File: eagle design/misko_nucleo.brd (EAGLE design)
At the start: 115 x 115 mm, 135 parts, among them CN1 LiPo Battery, IC1 MC1525TT, IC10 LTC4425, IC101 ADXL345, IC102 74HCT1G32GW, IC11 SP3012-04UTG, IC2 ORG1510-MK4, IC3 TPS63031, IC4 FT230XS, IC5 RN4678_BT_MODULE, IC6 FM25W256-SOIC, IC7 MICROSD_SPI_MODE, IC8 DS1394U-33+, IC9 MAX6818, Q1 ABM3B-8MHZ-10-1-U-T, Q2 BSS84, Q3 LFXTAL016178R, SW1 MICROJOYSTICK, SW2 PB6156RSL, SW3 PB6156RSL, U1 SN74LVC1G3157DBVR - BT switch, U2 ATMEGA1281-16AU, U3 TPS3808G33DBVT, U4 TMP36GRTZ, U5 MCP73871-2AAI/ML, U6 SN74LVC1G3157DBVR - GPS switch, X1 FH12-30S-0.5SH

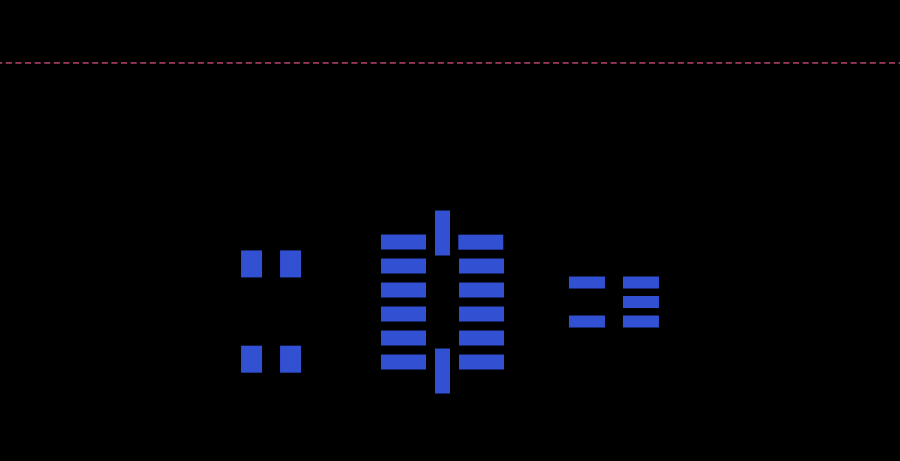
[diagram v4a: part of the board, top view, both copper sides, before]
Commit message: in main.c & sch/brd: - ditched dedicated SPI CS pullup resistors and switched to stm32 built-in pullups
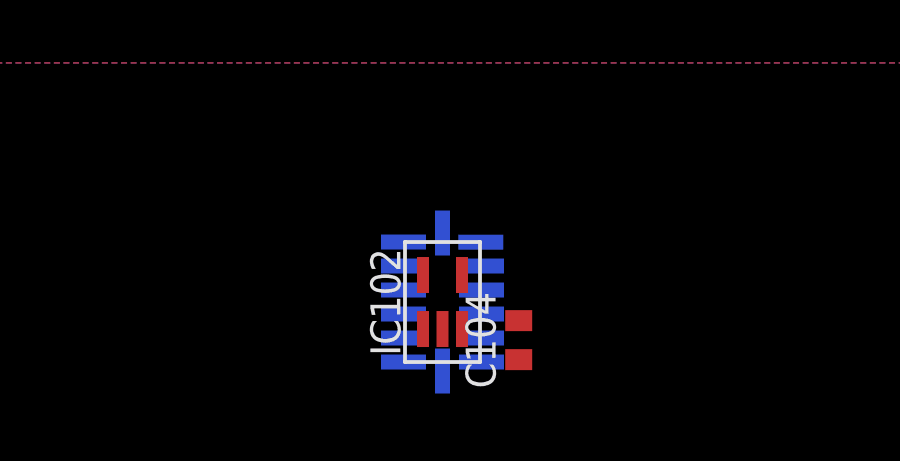
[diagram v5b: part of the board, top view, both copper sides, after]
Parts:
- removed R101: 10k, rcl:R0402
- moved C104 8.28 mm to (17.1, -15.2), flipped to the top, turned to 90 degrees
- moved IC102 5.71 mm to (14.6, -14.0), flipped to the top, turned to 0 degrees
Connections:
- net 3V3: no longer R101.2
- net ADXL345_CS: no longer R101.1
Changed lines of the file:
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@@
 <grid distance="25" unitdist="mil" unit="mm" style="lines" multiple="1" display="yes" altdistance="0.005" altunitdist="mm" altunit="mm"/>
 <layers>
-<layer number="1" name="Top" color="4" fill="1" visible="no" active="yes"/>
+<layer number="1" name="Top" color="4" fill="1" visible="yes" active="yes"/>
 <layer number="2" name="Route2" color="1" fill="3" visible="no" active="no"/>
 <layer number="3" name="Route3" color="4" fill="3" visible="no" active="no"/>
@@
 <layer number="19" name="Unrouted" color="6" fill="1" visible="yes" active="yes"/>
 <layer number="20" name="Dimension" color="14" fill="1" visible="yes" active="yes"/>
-<layer number="21" name="tPlace" color="7" fill="1" visible="no" active="yes"/>
+<layer number="21" name="tPlace" color="7" fill="1" visible="yes" active="yes"/>
 <layer number="22" name="bPlace" color="7" fill="1" visible="yes" active="yes"/>
-<layer number="23" name="tOrigins" color="15" fill="1" visible="no" active="yes"/>
+<layer number="23" name="tOrigins" color="15" fill="1" visible="yes" active="yes"/>
 <layer number="24" name="bOrigins" color="15" fill="1" visible="yes" active="yes"/>
 <layer number="25" name="tNames" color="7" fill="1" visible="no" active="yes"/>
-<layer number="26" name="bNames" color="7" fill="1" visible="yes" active="yes"/>
+<layer number="26" name="bNames" color="7" fill="1" visible="no" active="yes"/>
 <layer number="27" name="tValues" color="7" fill="1" visible="no" active="yes"/>
 <layer number="28" name="bValues" color="7" fill="1" visible="no" active="yes"/>
 <layer number="29" name="tStop" color="7" fill="3" visible="no" active="yes"/>
-<layer number="30" name="bStop" color="7" fill="6" visible="yes" active="yes"/>
+<layer number="30" name="bStop" color="7" fill="6" visible="no" active="yes"/>
 <layer number="31" name="tCream" color="7" fill="4" visible="no" active="yes"/>
 <layer number="32" name="bCream" color="7" fill="5" visible="no" active="yes"/>
@@
 <layer number="37" name="tTest" color="7" fill="1" visible="no" active="yes"/>
 <layer number="38" name="bTest" color="7" fill="1" visible="no" active="yes"/>
-<layer number="39" name="tKeepout" color="4" fill="11" visible="no" active="yes"/>
+<layer number="39" name="tKeepout" color="4" fill="11" visible="yes" active="yes"/>
 <layer number="40" name="bKeepout" color="1" fill="11" visible="yes" active="yes"/>
-<layer number="41" name="tRestrict" color="4" fill="10" visible="no" active="yes"/>
+<layer number="41" name="tRestrict" color="4" fill="10" visible="yes" active="yes"/>
 <layer number="42" name="bRestrict" color="1" fill="10" visible="yes" active="yes"/>
 <layer number="43" name="vRestrict" color="2" fill="10" visible="yes" active="yes"/>
@@
 <layer number="49" name="Reference" color="7" fill="1" visible="no" active="yes"/>
 <layer number="50" name="dxf" color="7" fill="1" visible="no" active="no"/>
-<layer number="51" name="tDocu" color="7" fill="1" visible="no" active="yes"/>
+<layer number="51" name="tDocu" color="7" fill="1" visible="yes" active="yes"/>
 <layer number="52" name="bDocu" color="7" fill="1" visible="yes" active="yes"/>
 <layer number="53" name="tGND_GNDA" color="7" fill="9" visible="no" active="no"/>
@@
 <attribute name="VALUE" x="0" y="0" size="1.27" layer="27" align="top-left"/>
 </element>
-<element name="C104" library="rcl" package="C0402" value="0.1u / 16V" x="8.89" y="-15.875" smashed="yes" rot="MR0">
-<attribute name="NAME" x="8.89" y="-14.605" size="1" layer="26" rot="MR0" align="center"/>
-<attribute name="VALUE" x="10.16" y="-18.415" size="1.27" layer="28" rot="MR0"/>
+<element name="C104" library="rcl" package="C0402" value="0.1u / 16V" x="17.145" y="-15.24" smashed="yes" rot="R90">
+<attribute name="NAME" x="15.875" y="-15.24" size="1" layer="25" rot="R90" align="center"/>
+<attribute name="VALUE" x="19.685" y="-16.51" size="1.27" layer="27" rot="R90"/>
 </element>
 <element name="IC101" library="ADXL345 Accelerometer" package="LGA14" value="ADXL345" x="14.605" y="-13.97" smashed="yes" rot="MR0">
@@
 <attribute name="VALUE" x="14.605" y="-17.72" size="1" layer="28" rot="MR0" align="center"/>
 </element>
-<element name="IC102" library="74HCT1G32GW - OR Gate" package="SOT353/5" value="74HCT1G32GW" x="20.32" y="-13.97" smashed="yes" rot="MR270">
-<attribute name="NAME" x="20.32" y="-12.065" size="1" layer="26" font="vector" rot="MR0" align="center"/>
-<attribute name="VALUE" x="20.32" y="-15.97" size="1" layer="28" font="vector" rot="MR0" align="center"/>
-</element>
-<element name="R101" library="rcl" package="R0402" value="10k" x="8.89" y="-12.7" smashed="yes" rot="MR0">
-<attribute name="NAME" x="8.89" y="-11.43" size="1" layer="26" rot="MR0" align="center"/>
-<attribute name="VALUE" x="9.525" y="-15.24" size="1.27" layer="28" rot="MR0"/>
+<element name="IC102" library="74HCT1G32GW - OR Gate" package="SOT353/5" value="74HCT1G32GW" x="14.605" y="-13.97" smashed="yes">
+<attribute name="NAME" x="12.7" y="-13.97" size="1" layer="25" font="vector" rot="R90" align="center"/>
+<attribute name="VALUE" x="16.605" y="-13.97" size="1" layer="27" font="vector" rot="R90" align="center"/>
 </element>
 </elements>
@@
 <contactref element="C104" pad="2"/>
 <contactref element="IC102" pad="GND"/>
-<wire x1="15.905" y1="-15.17" x2="8.24" y2="-15.875" width="0" layer="19" extent="16-16"/>
-<wire x1="15.905" y1="-14.37" x2="15.905" y2="-15.17" width="0" layer="19" extent="16-16"/>
+<wire x1="15.905" y1="-14.37" x2="17.145" y2="-14.59" width="0" layer="19" extent="16-16"/>
+<wire x1="15.905" y1="-15.17" x2="15.905" y2="-14.37" width="0" layer="19" extent="16-16"/>
+<wire x1="15.255" y1="-14.87" x2="15.905" y2="-15.17" width="0" layer="19" extent="1-16"/>
 <wire x1="15.905" y1="-12.77" x2="15.905" y2="-14.37" width="0" layer="19" extent="16-16"/>
-<wire x1="21.22" y1="-14.62" x2="15.905" y2="-14.37" width="0" layer="19" extent="16-16"/>
 <wire x1="5.79" y1="25.36" x2="15.905" y2="-12.77" width="0" layer="19" extent="16-16"/>
 <wire x1="90.25" y1="18" x2="66.75" y2="12.66" width="0" layer="19" extent="1-1"/>
@@
 <contactref element="IC101" pad="VCC"/>
 <contactref element="IC102" pad="VCC"/>
-<contactref element="R101" pad="2"/>
 <wire x1="15.881" y1="-11.975" x2="11.43" y2="33.02" width="0" layer="19" extent="1-16"/>
-<wire x1="19.42" y1="-13.32" x2="15.881" y2="-11.975" width="0" layer="19" extent="16-16"/>
-<wire x1="15.905" y1="-15.97" x2="15.881" y2="-11.975" width="0" layer="19" extent="16-16"/>
-<wire x1="9.54" y1="-15.875" x2="15.905" y2="-15.97" width="0" layer="19" extent="16-16"/>
-<wire x1="8.24" y1="-12.7" x2="9.54" y2="-15.875" width="0" layer="19" extent="16-16"/>
+<wire x1="13.955" y1="-13.07" x2="15.881" y2="-11.975" width="0" layer="19" extent="1-16"/>
+<wire x1="15.905" y1="-15.97" x2="13.955" y2="-13.07" width="0" layer="19" extent="1-16"/>
+<wire x1="17.145" y1="-15.89" x2="15.905" y2="-15.97" width="0" layer="19" extent="16-16"/>
 </signal>
 <signal name="NRST" class="2">
@@
 <contactref element="IC101" pad="!CS!"/>
 <contactref element="IC102" pad="A"/>
-<contactref element="R101" pad="1"/>
-<wire x1="21.22" y1="-13.97" x2="56.515" y2="33.02" width="0" layer="19" extent="1-16"/>
-<wire x1="14.605" y1="-16.27" x2="21.22" y2="-13.97" width="0" layer="19" extent="16-16"/>
-<wire x1="9.54" y1="-12.7" x2="14.605" y2="-16.27" width="0" layer="19" extent="16-16"/>
+<wire x1="14.605" y1="-14.87" x2="56.515" y2="33.02" width="0" layer="19" extent="1-1"/>
+<wire x1="14.605" y1="-16.27" x2="14.605" y2="-14.87" width="0" layer="19" extent="1-16"/>
 </signal>
 <signal name="GPS_WKUP" class="2">
@@
 <wire x1="56.555" y1="15.2" x2="56.515" y2="15.24" width="0.25" layer="1"/>
 <contactref element="IC102" pad="B"/>
-<wire x1="21.22" y1="-13.32" x2="56.515" y2="15.24" width="0" layer="19" extent="1-16"/>
+<wire x1="13.955" y1="-14.87" x2="56.515" y2="15.24" width="0" layer="19" extent="1-1"/>
 </signal>
 <signal name="PB6" class="2">
@@
 <contactref element="IC101" pad="SDA"/>
 <contactref element="IC102" pad="Y"/>
-<wire x1="13.305" y1="-11.97" x2="19.42" y2="-14.62" width="0" layer="19" extent="16-16"/>
+<wire x1="15.255" y1="-13.07" x2="13.305" y2="-11.97" width="0" layer="19" extent="1-16"/>
 </signal>
 <signal name="ADXL345:ADXL345_INT2">

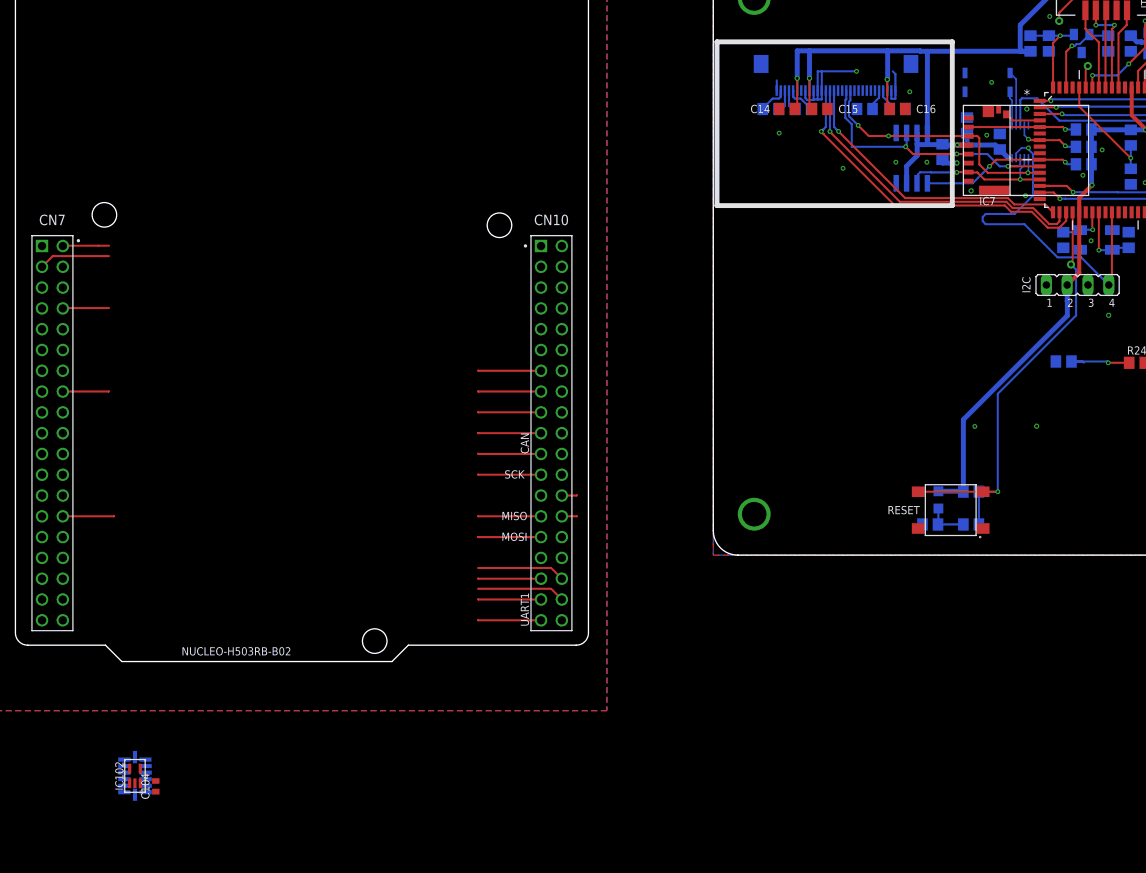
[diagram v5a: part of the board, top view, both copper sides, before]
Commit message: in brd & sch: - added FeRAM module
- created and tested fm25w256 driver
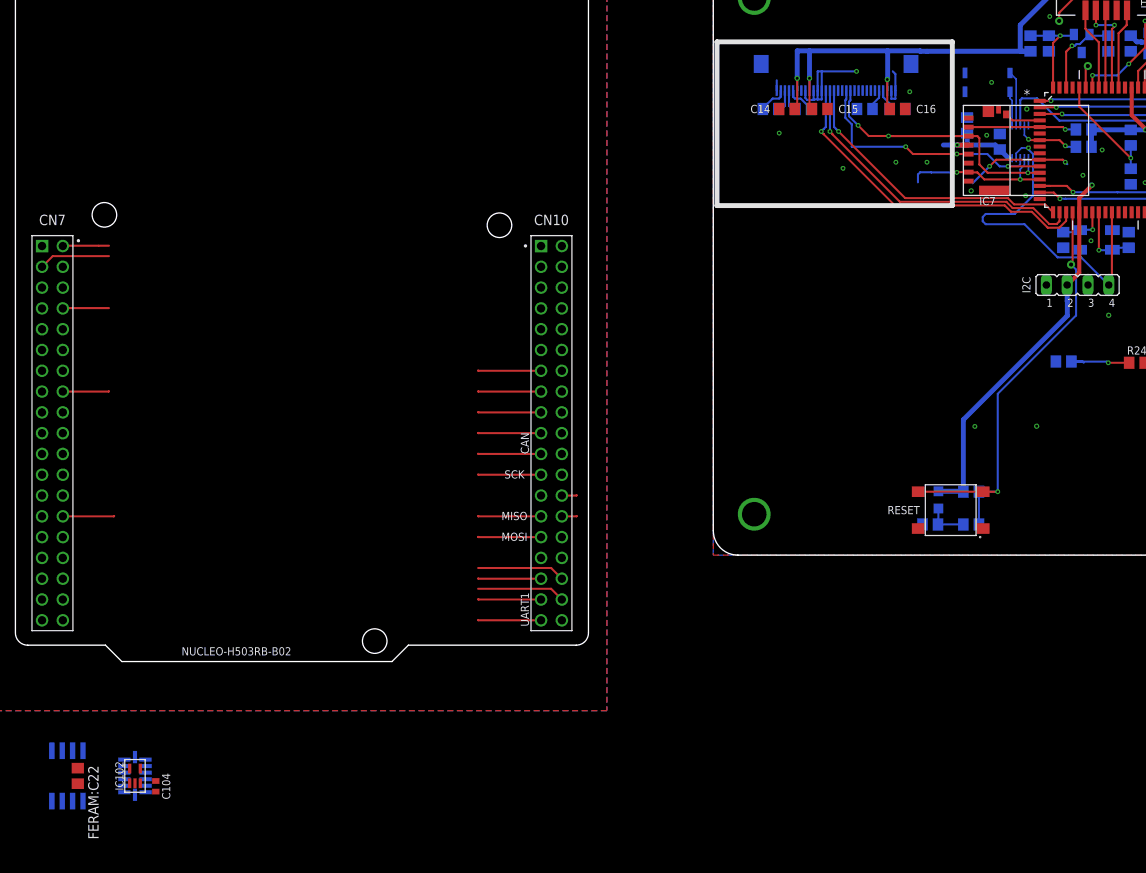
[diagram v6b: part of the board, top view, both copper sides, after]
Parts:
- removed C22: 0.1µF, rcl:C0805
- removed IC6: FM25W256-SOIC, FM25W256 FERAM:SOIC08
- removed R18: 10k, rcl:R0805
- added FERAM:C22: 0.1u / 16V, rcl:C0805
- added FERAM:IC1: FM25W256, FM25W256 FERAM:SOIC08
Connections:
- removed net SPI_FRAM_CS: BRD1.CN10_13
- new net SPI1_FRAM_CS: BRD1.CN10_13, FERAM:IC1.!CS!
- net 3V3: now also FERAM:C22.1, FERAM:IC1.!HOLD!, FERAM:IC1.!WP!, FERAM:IC1.VCC
- net GND: now also FERAM:C22.2, FERAM:IC1.GND; no longer C22.2, IC6.GND
- net SPI1_MISO: now also FERAM:IC1.SO
- net SPI1_MOSI: now also FERAM:IC1.SI
- net SPI1_SCK: now also FERAM:IC1.SCK
- net SPI_MISO_PIN: no longer IC6.SO
- net SPI_MOSI_PIN: no longer IC6.SI
- net SPI_SCK_PIN: no longer IC6.SCK
- net SPI_SS_FRAM_PIN: no longer IC6.!CS!, R18.1
- net VCC: no longer C22.1, IC6.!HOLD!, IC6.!WP!, IC6.VCC, R18.2
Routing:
- net VCC: track 448.3 -> 422.3 mm
- net SPI_FRAM_CS: track 7.71 -> 0.00 mm
- net SPI1_FRAM_CS: track 0.00 -> 7.71 mm
- net SPI_SS_FRAM_PIN: track 19.7 -> 13.0 mm
- net GND: track 49.4 -> 47.2 mm, vias 44 -> 43
- net SPI_SCK_PIN: track 36.9 -> 35.3 mm
- net SPI_MOSI_PIN: track 34.3 -> 33.7 mm

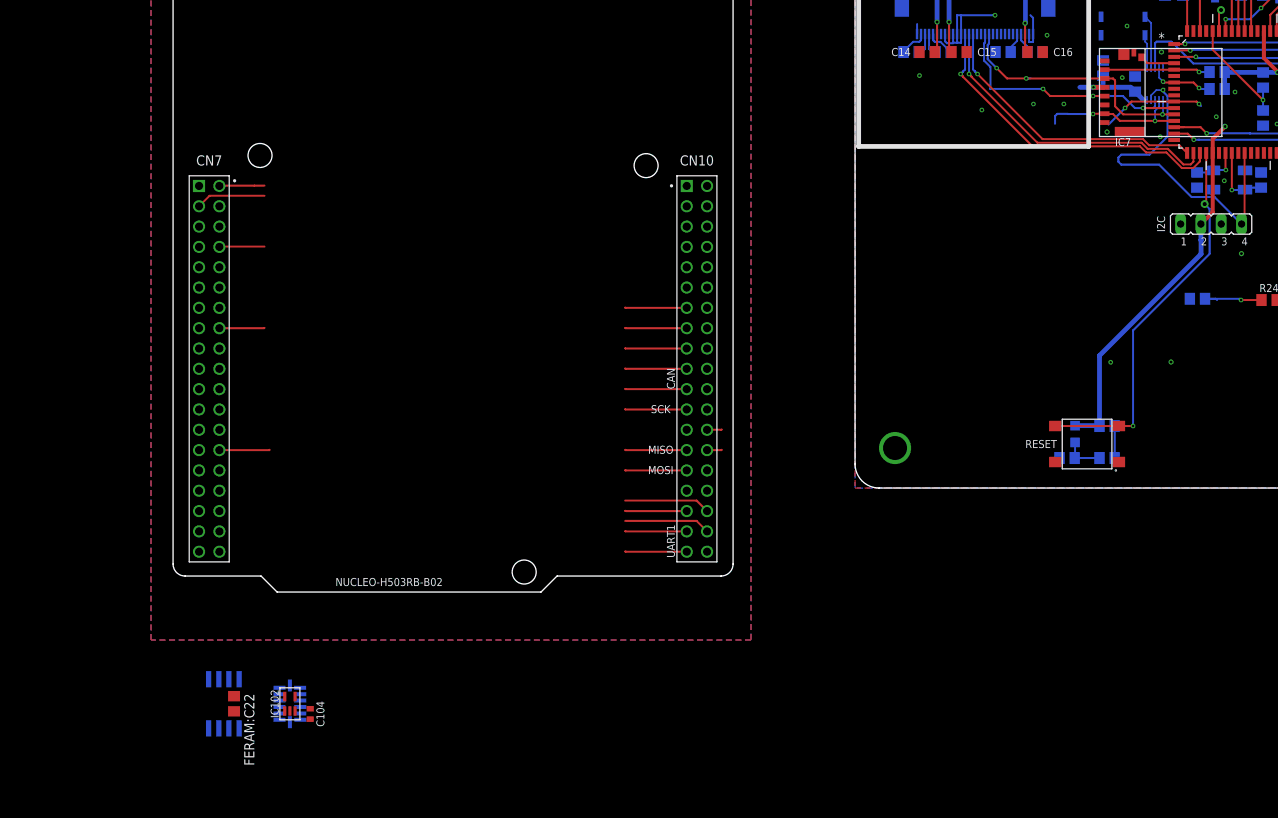
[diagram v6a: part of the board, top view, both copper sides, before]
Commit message: in sch & brd: - updated SD card module library - added SD card module to sch
- added ST's FileX middleware
- added sd.c/.h skeleton
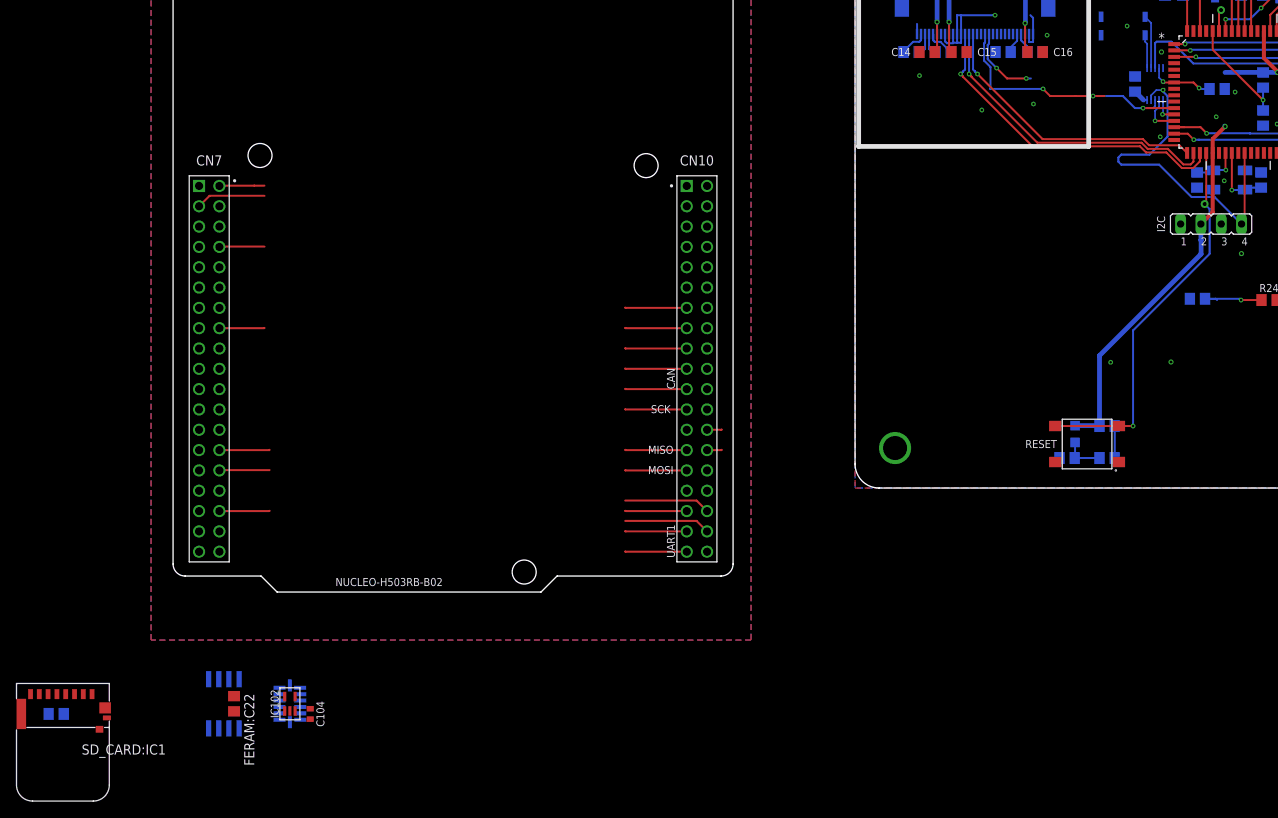
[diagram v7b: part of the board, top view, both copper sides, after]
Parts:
- removed C31: 0.1µF, rcl:C0805
- removed IC7: MICROSD_SPI_MODE, Molex SD-47309 SD Card Slot:MICRO_SD_CONNECTOR
- removed R37: 10k, rcl:R0805
- added SD_CARD:C31: 0.1u / 16V, rcl:C0805
- added SD_CARD:IC1: 47309-2651, Molex SD-47309 SD Card Slot:MICRO_SD_CONNECTOR
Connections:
- removed net PA1: BRD1.CN7_30
- removed net PB0: BRD1.CN7_34
- new net SD_CD: BRD1.CN7_34, SD_CARD:IC1.POL
- new net SPI1_SD_CS: BRD1.CN7_30, SD_CARD:IC1.CD/DAT3
- net 3V3: now also SD_CARD:C31.1, SD_CARD:IC1.DET, SD_CARD:IC1.VDD
- net GND: now also SD_CARD:C31.2, SD_CARD:IC1.GND1, SD_CARD:IC1.GND2, SD_CARD:IC1.GND3; no longer C31.2, IC7.GND2, IC7.GND4, IC7.POL, IC7.VSS
- net SD_CARD_DETECT_PIN: no longer IC7.DET
- net SPI1_MISO: now also SD_CARD:IC1.CMD, SD_CARD:IC1.DAT0
- net SPI1_SCK: now also SD_CARD:IC1.CLK
- net SPI_MISO_PIN: no longer IC7.DAT0
- net SPI_MOSI_PIN: no longer IC7.CMD
- net SPI_SCK_PIN: no longer IC7.CLK
- net SPI_SS_SD_CARD_PIN: no longer IC7.CD/DAT3, R37.1
- net VCC: no longer C31.1, IC7.VDD, R37.2
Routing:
- net SPI_MOSI_PIN: track 33.7 -> 12.9 mm
- net SPI_MISO_PIN: track 19.2 -> 5.19 mm, vias 2 -> 1
- net SPI_SS_SD_CARD_PIN: track 13.7 -> 0.34 mm, vias 1 -> 0
- net SPI_SS_FRAM_PIN: track 13.0 -> 0.00 mm, vias 2 -> 0
- net VCC: track 422.3 -> 410.1 mm, vias 17 -> 16
- net SD_CD: track 0.00 -> 6.29 mm
- net SPI1_SD_CS: track 0.00 -> 6.29 mm
- net SD_CARD_DETECT_PIN: track 4.36 -> 0.00 mm
- net GND: vias 43 -> 40
